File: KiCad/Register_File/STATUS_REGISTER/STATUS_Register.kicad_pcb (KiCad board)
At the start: 2 copper layers, 100 x 100 mm, 40 parts, among them J1 Conn_01x02_Pin, J10 Conn_01x02_Pin, J11 Conn_01x04_Pin, J2 Conn_01x02_Pin, J3 Conn_01x02_Pin, J4 Conn_01x08_Pin, J6 Conn_01x04_Pin, J7 Conn_01x04_Pin, SW1 SW_SPDT, U1 74LS173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

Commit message: finished registier file boards
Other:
- board text added: "Status Register"
- board text removed: "SR Register"
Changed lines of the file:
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@@
 	(gr_poly
 		(pts
-			(xy 173.6 55) (xy 173.6 70) (xy 190 70) (xy 190 65.1) (xy 193 62.1) (xy 193 55)
+			(xy 166.5 55) (xy 166.5 70) (xy 191 70) (xy 191 55)
 		)
 		(stroke
@@
 	)
 	(gr_text "rev 1.0"
-		(at 174 65.3 0)
+		(at 166.85 65.35 0)
 		(layer "F.SilkS")
 		(effects
@@
 	)
 	(gr_text "25/9/24"
-		(at 174 68.7 0)
+		(at 166.85 68.75 0)
 		(layer "F.SilkS")
 		(effects
@@
 	)
 	(gr_text "SH8"
-		(at 174 58.2 0)
+		(at 166.85 58.25 0)
 		(layer "F.SilkS")
 		(effects
@@
 		)
 	)
-	(gr_text "SR Register"
-		(at 174 61.7 0)
-		(layer "F.SilkS")
-		(effects
+	(gr_text "Status Register"
+		(at 166.85 61.75 0)
+		(layer "F.SilkS")
+		(effects

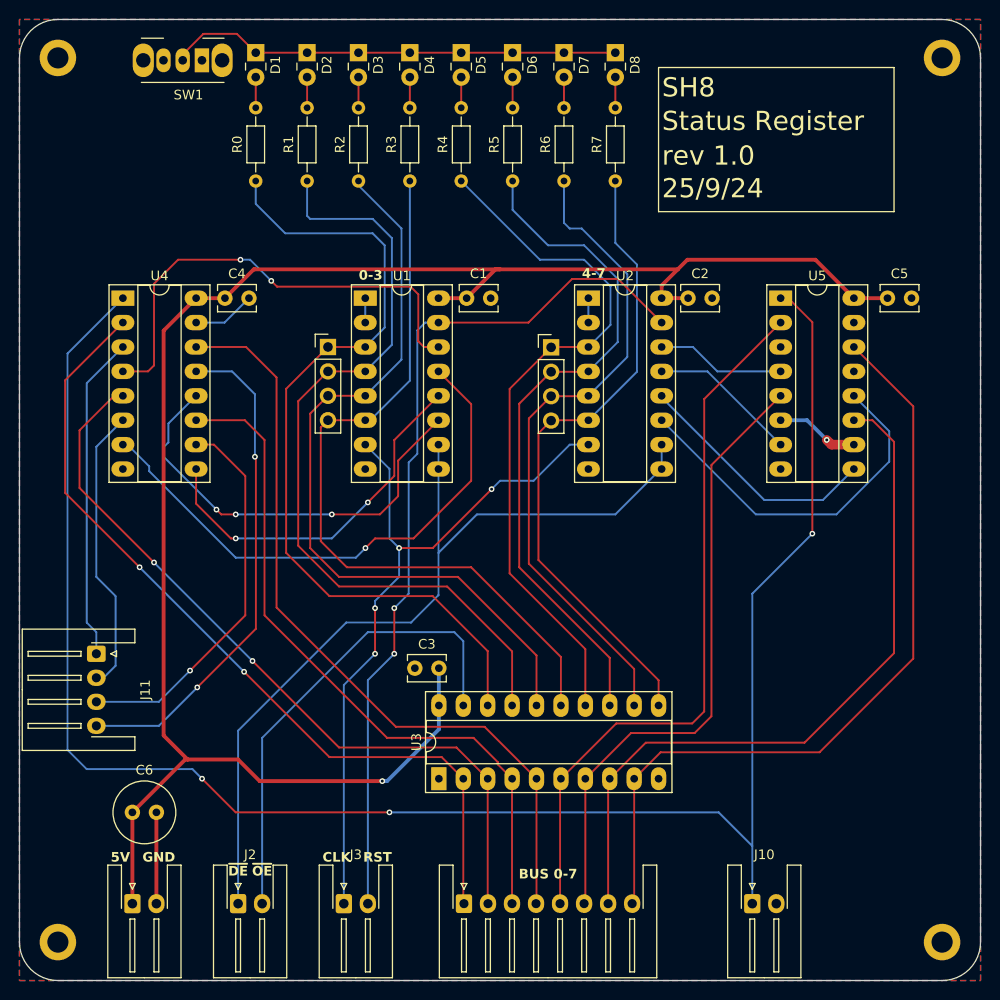
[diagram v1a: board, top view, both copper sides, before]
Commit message: added con_ctrl board mdr_mar
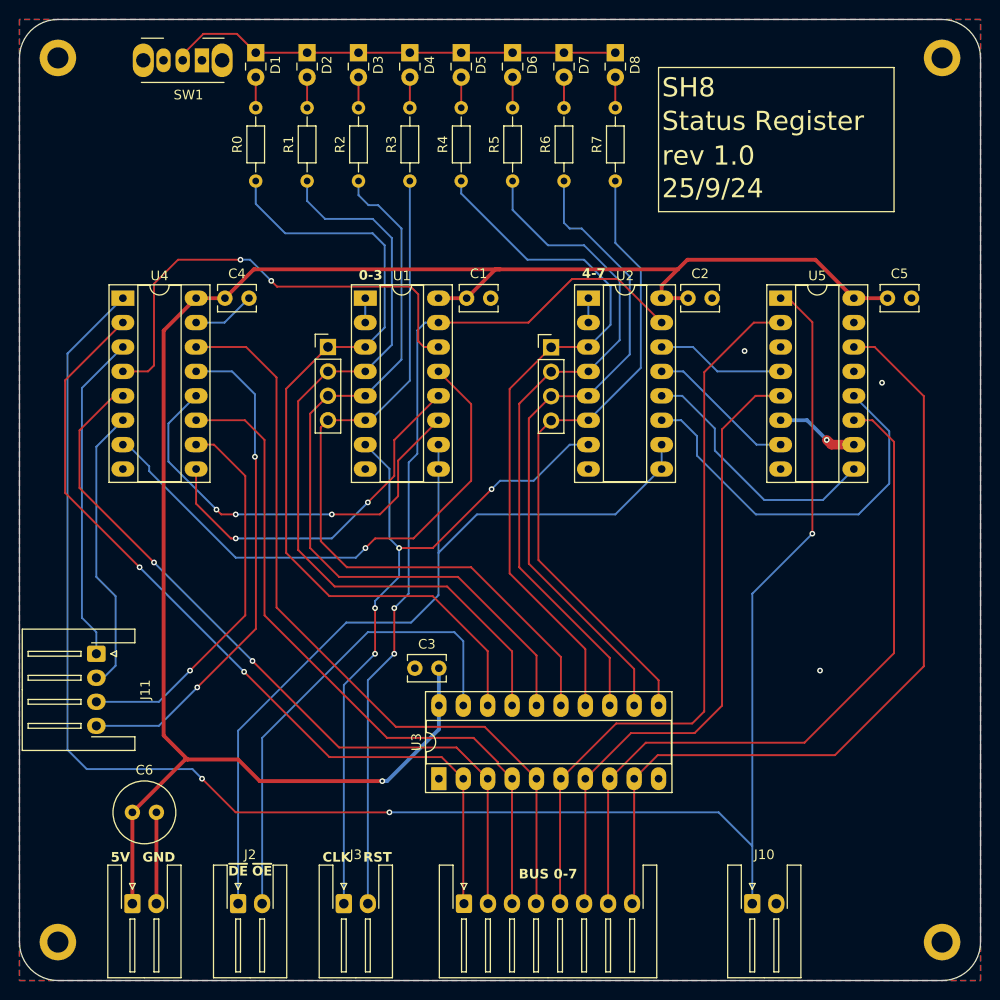
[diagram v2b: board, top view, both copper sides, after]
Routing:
- net /B7: track 82.3 -> 85.6 mm
- net Net-(U2-D3): track 38.4 -> 40.9 mm
- net /B4: track 74.6 -> 76.2 mm
- net /B5: track 65.2 -> 66.7 mm
- net Net-(U2-D2): track 25.9 -> 27.2 mm
- net /Y4: track 73.6 -> 74.3 mm
- net /Y1: track 84.2 -> 83.5 mm
- net /Y2: track 79.6 -> 80.2 mm
- net GND: vias 1 -> 4
